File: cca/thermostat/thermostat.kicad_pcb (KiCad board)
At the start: 2 copper layers, 15 parts, among them K1 TX2-LT-5V-TH, K2 TX2-LT-5V-TH, K3 TX2-LT-5V-TH, Q1 2N3904, Q2 2N3904, Q3 2N3904, Q4 2N3904, Q5 2N3904, Q6 2N3904

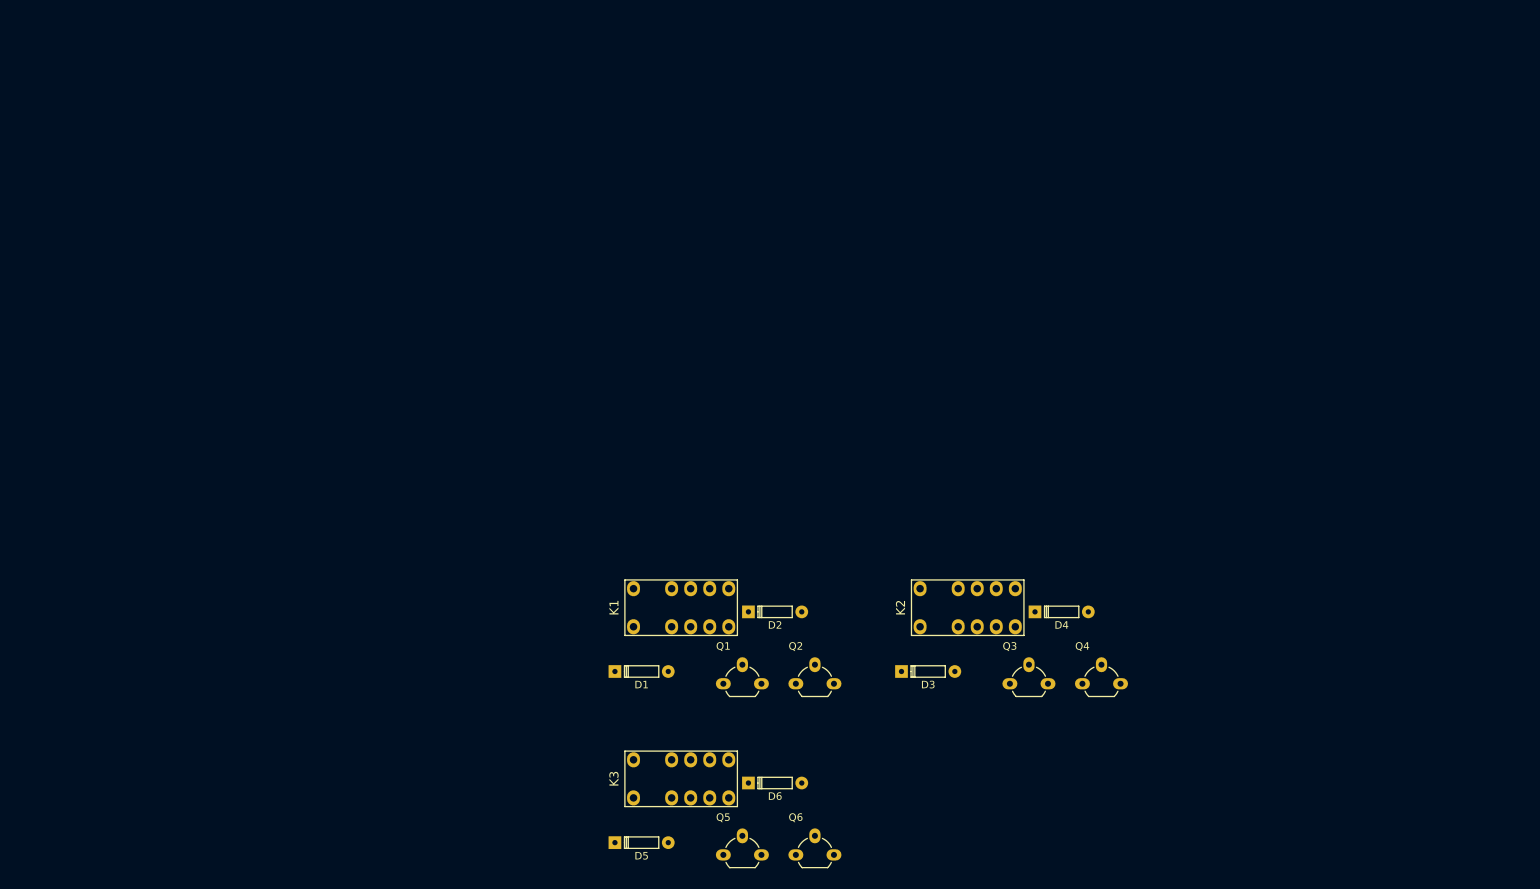
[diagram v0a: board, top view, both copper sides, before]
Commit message: Prelim schem. TODO: battery backup, layout
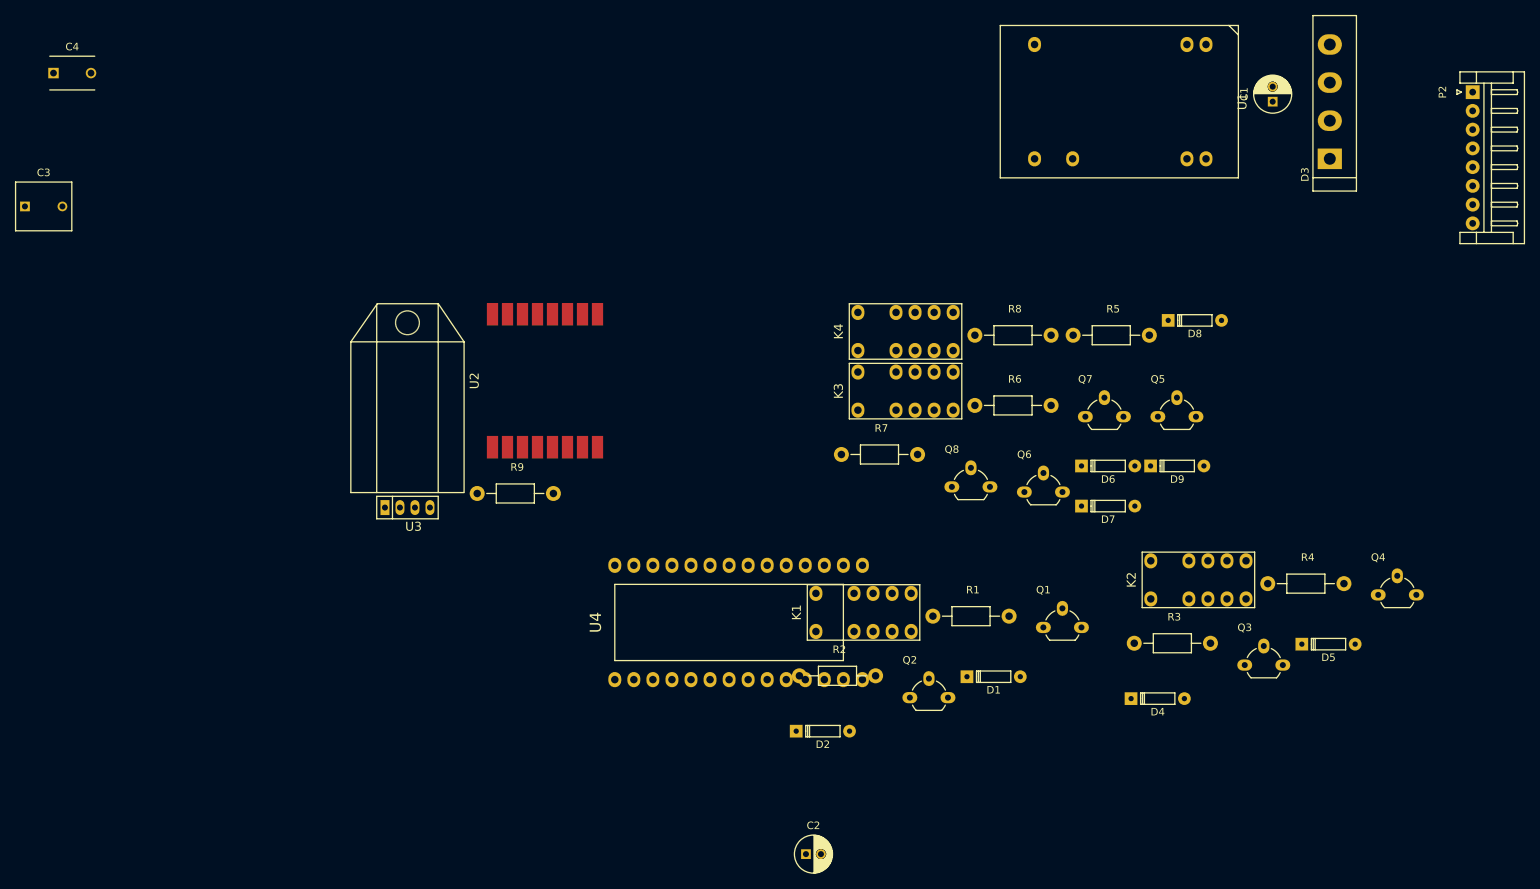
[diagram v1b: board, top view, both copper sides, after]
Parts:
- added C1: 47uF/63V, Capacitors_ThroughHole:C_Radial_D5_L11_P2, F.Cu at (233.7, 27.9)
- added C2: 10uF/16V, Capacitors_ThroughHole:C_Radial_D5_L11_P2, F.Cu at (171.4, 128.3)
- added C3: 1uF, Capacitors_ThroughHole:C_Rect_L7.5_W6.5_P5, F.Cu at (67.3, 41.9)
- added C4: 0.1uF, Capacitors_ThroughHole:C_Disc_D6_P5, F.Cu at (71.1, 24.1)
- added D7: 1N4148, t_footprints:DO-35, F.Cu at (208.2, 81.9)
- added D8: 1N4148, t_footprints:DO-35, F.Cu at (219.7, 57.1)
- added D9: 1N4148, t_footprints:DO-35, F.Cu at (217.4, 76.5)
- added K4: TX2-LT-5V-TH, t_footprints:RELAY_2_FORM_C, F.Cu at (178.4, 61.1)
- added P2: tstat_cable_con, JST_EH_RIGHT_8pin, F.Cu at (260.4, 26.7)
- added Q7: 2N3904, TO_SOT_Packages_THT:TO-92_Molded_Wide_Oval, F.Cu at (208.7, 69.9)
- added Q8: 2N3904, TO_SOT_Packages_THT:TO-92_Molded_Wide_Oval, F.Cu at (190.9, 79.3)
- added R1: 4.75k, Resistors_ThroughHole:Resistor_Horizontal_RM10mm, F.Cu at (188.4, 96.5)
- added R2: 4.75k, Resistors_ThroughHole:Resistor_Horizontal_RM10mm, F.Cu at (170.6, 104.5)
- added R3: 4.75K, Resistors_ThroughHole:Resistor_Horizontal_RM10mm, F.Cu at (215.2, 100.2)
- added R4: 4.75K, Resistors_ThroughHole:Resistor_Horizontal_RM10mm, F.Cu at (233.0, 92.2)
- added R5: 4.75K, Resistors_ThroughHole:Resistor_Horizontal_RM10mm, F.Cu at (207.1, 59.1)
- added R6: 4.75K, Resistors_ThroughHole:Resistor_Horizontal_RM10mm, F.Cu at (194.0, 68.4)
- added R7: 4.75K, Resistors_ThroughHole:Resistor_Horizontal_RM10mm, F.Cu at (176.2, 75.0)
- added R8: 4.75K, Resistors_ThroughHole:Resistor_Horizontal_RM10mm, F.Cu at (194.0, 59.1)
- added R9: 4.75K, Resistors_ThroughHole:Resistor_Horizontal_RM10mm, F.Cu at (127.6, 80.2)
- added U1: DJ06S4805A, DJ06S4805A, F.Cu at (224.8, 20.3)
- added U2: RFM69W, RFM69W, F.Cu at (129.7, 74.0)
- added U3: DHT22, DHT22, F.Cu at (115.3, 82.1)
- added U4: TEENSY-LC, Teensy-3.2, F.Cu at (148.5, 105.0)
- D3: value 1N4148 -> GBU806; footprint t_footprints:DO-35 -> GBU
- moved D5 95.3 mm to (237.6, 100.3)
- moved D3 89.1 mm to (241.3, 35.6), turned to 90 degrees
- moved Q5 82.3 mm to (218.4, 69.9)
- moved D6 61.3 mm to (208.2, 76.5)
- moved K3 59.7 mm to (178.4, 69.1)
- moved Q6 57.2 mm to (200.6, 80.0)
- moved D1 46.9 mm to (192.9, 104.6)
- moved Q1 43.3 mm to (203.1, 98.0)
- moved Q4 41.2 mm to (247.8, 93.7)
- moved Q3 31.4 mm to (230.0, 103.1)
- moved K2 31.0 mm to (217.4, 94.2)
- moved K1 24.3 mm to (172.8, 98.6)
- moved D4 17.3 mm to (214.8, 107.5)
- moved D2 17.1 mm to (170.1, 111.9)
- moved Q2 15.3 mm to (185.3, 107.4)
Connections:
- net /relay_heat.sch/R-COM renamed Net-(K3-Pad4)
- net /relay_heat.sch/R-NO renamed Net-(K3-Pad5)
- D3 pad 1: +5V -> Net-(C1-Pad1)
- D3 pad 2: Net-(D3-Pad2) -> /power/24VAC_2
- K1 pad 4: /relay_fan.sch/R-COM -> /power/24VAC_1
- K1 pad 5: /relay_fan.sch/R-NO -> /relay_fan/G
- K2 pad 12: Net-(D4-Pad2) -> Net-(D5-Pad2)
- K2 pad 4: /relay_cool.sch/R-COM -> /power/24VAC_1
- K2 pad 5: /relay_cool.sch/R-NO -> /relay_emheat/E
- K2 pad 7: Net-(D3-Pad2) -> Net-(D4-Pad2)
- K3 pad 1: +5V -> Net-(D6-Pad2)
- K3 pad 12: Net-(D6-Pad2) -> +5V
- K3 pad 6: +5V -> Net-(D8-Pad2)
- K3 pad 7: Net-(D5-Pad2) -> +5V
- K3 pad 9: Net-(K3-Pad9) -> /power/24VAC_1
- Q3 pad 3: Net-(D3-Pad2) -> Net-(D4-Pad2)
- Q4 pad 3: Net-(D4-Pad2) -> Net-(D5-Pad2)
- Q5 pad 3: Net-(D5-Pad2) -> Net-(D6-Pad2)
- Q6 pad 3: Net-(D6-Pad2) -> Net-(D7-Pad2)

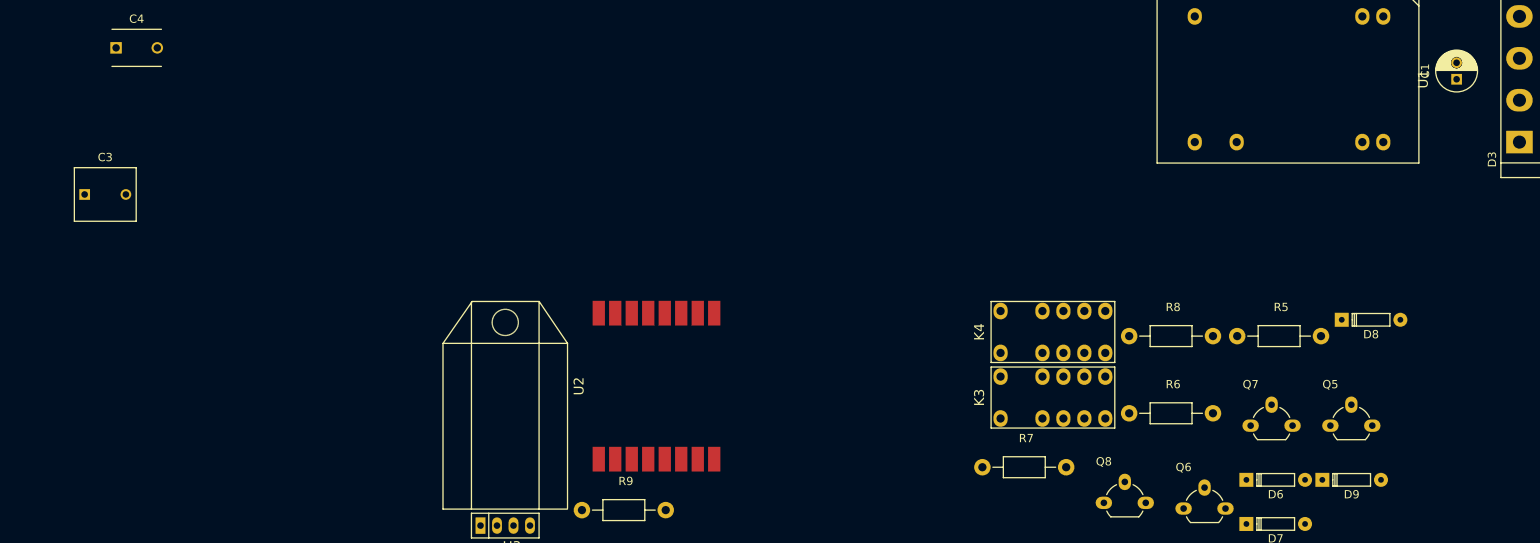
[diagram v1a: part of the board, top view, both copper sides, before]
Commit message: cap cleanup pass, fully qualify footprints
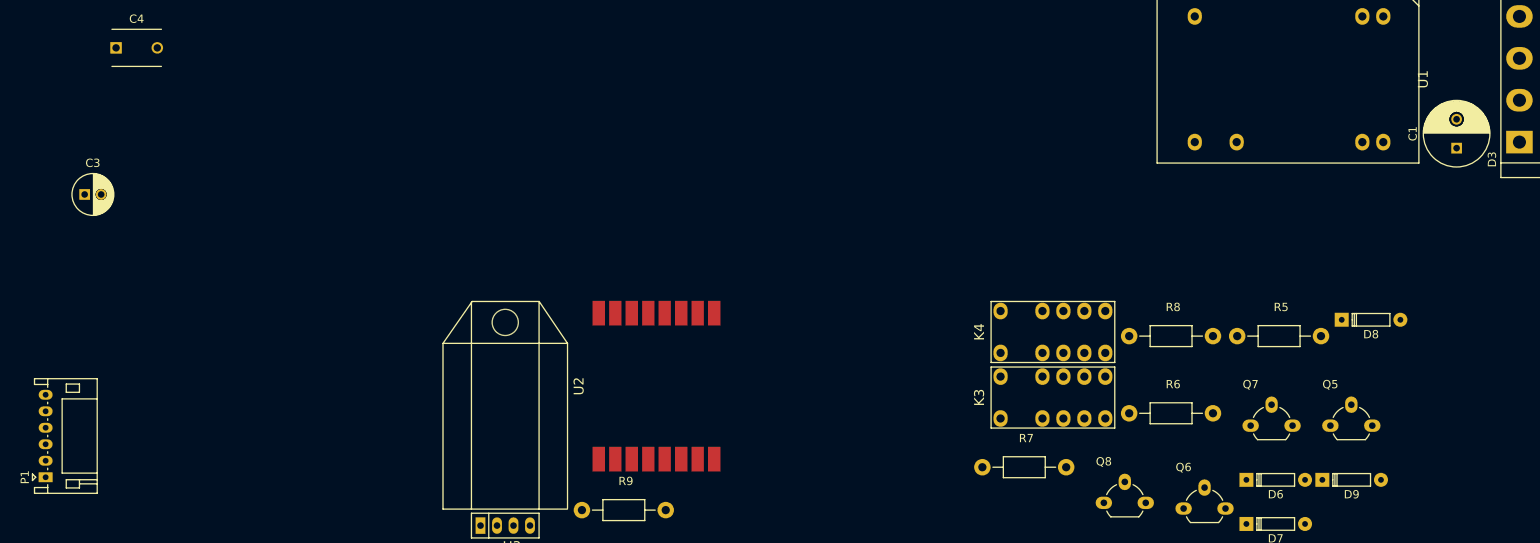
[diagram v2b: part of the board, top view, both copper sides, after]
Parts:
- added P1: tstat_ui_conn, t_footprints:JST_PH_RIGHT_6pin, F.Cu at (62.6, 76.2)
- C1: footprint Capacitors_ThroughHole:C_Radial_D5_L11_P2 -> t_footprints:C_Radial_D8_L15_P3.5
- C2: value 10uF/16V -> ESK106M016AC3AA; footprint Capacitors_ThroughHole:C_Radial_D5_L11_P2 -> t_footprints:C_Radial_D5_L12.5_P2
- C3: value 1uF -> 10uF/16V; footprint Capacitors_ThroughHole:C_Rect_L7.5_W6.5_P5 -> t_footprints:C_Radial_D5_L12.5_P2
- C4: value 0.1uF -> 0.1uF/50V
- D3: footprint GBU -> t_footprints:GBU
- P2: footprint JST_EH_RIGHT_8pin -> t_footprints:JST_EH_RIGHT_8pin
- moved C1 8.35 mm to (233.7, 36.3)
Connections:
- K1 pad 10: Net-(K1-Pad10) -> (no net)
- K1 pad 3: Net-(K1-Pad3) -> (no net)
- K1 pad 8: Net-(K1-Pad8) -> (no net)
- K1 pad 9: Net-(K1-Pad9) -> (no net)
- K2 pad 10: Net-(K2-Pad10) -> (no net)
- K2 pad 3: Net-(K2-Pad3) -> (no net)
- K2 pad 8: Net-(K2-Pad8) -> (no net)
- K2 pad 9: Net-(K2-Pad9) -> (no net)
- K3 pad 10: Net-(K3-Pad10) -> (no net)
- K3 pad 3: Net-(K3-Pad3) -> (no net)
- K3 pad 4: Net-(K3-Pad4) -> (no net)
- K3 pad 5: Net-(K3-Pad5) -> (no net)
- U1 pad 11: Net-(U1-Pad11) -> (no net)
- U2 pad 10: /control_comm/ant -> (no net)
- U2 pad 3: Net-(U2-Pad3) -> (no net)
- U2 pad 4: Net-(U2-Pad4) -> (no net)
- U2 pad 5: Net-(U2-Pad5) -> (no net)
- U2 pad 6: Net-(U2-Pad6) -> (no net)
- U2 pad 7: Net-(U2-Pad7) -> (no net)
- U3 pad 3: Net-(U3-Pad3) -> (no net)
- U4 pad 14: Net-(U4-Pad14) -> (no net)
- U4 pad 15: Net-(U4-Pad15) -> (no net)
- U4 pad 2: Net-(U4-Pad2) -> (no net)
- U4 pad 5: Net-(U4-Pad5) -> (no net)
- U4 pad 6: Net-(U4-Pad6) -> (no net)
- U4 pad 7: Net-(U4-Pad7) -> (no net)
- U4 pad 8: Net-(U4-Pad8) -> (no net)
- U4 pad 9: Net-(U4-Pad9) -> (no net)

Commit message: cleanup pass after clean checkout
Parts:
- C2: value ESK106M016AC3AA -> 10uF/16V
- moved C1 0.73 mm to (233.7, 35.6)
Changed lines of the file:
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@@
     (links 105)
     (no_connects 105)
-    (area 0 0 0 0)
+    (area 59.105 15.884999 269.553 133.145)
     (thickness 1.6)
     (drawings 0)
@@
   )
   (module t_footprints:C_Radial_D8_L15_P3.5 (layer F.Cu)
-    (at 233.68 36.29 90)
+    (at 233.68 35.56 90)
     (descr "Radial Electrolytic Capacitor Diameter 8mm x Length 15mm, Pitch 3.5mm")
     (tags "Electrolytic Capacitor")
@@
       (effects (font (size 1 1) (thickness 0.15)))
     )
-    (fp_text value ESK106M016AC3AA (at 1 3.8) (layer F.Fab)
-      (effects (font (size 1 1) (thickness 0.15)))
-    )
+    (fp_text value 10uF/16V (at 1 3.8) (layer F.Fab)
+      (effects (font (size 1 1) (thickness 0.15)))
+    )

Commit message: thermostat... wip many updates
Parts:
- added AE1: ANTENNA_915, t_footprints:ant_915_dipole_conn, F.Cu at (0.00, 0.00)
- P1: moved to B.Cu
- U1: footprint DJ06S4805A -> t_footprints:DJ06S4805A
- U2: footprint RFM69W -> t_footprints:RFM69W
- U3: footprint DHT22 -> t_footprints:DHT22
- U4: footprint Teensy-3.2 -> t_footprints:Teensy-3.2; moved to B.Cu
- moved U4 93.6 mm to (118.1, 16.5)
- moved P1 91.7 mm to (119.7, 4.45), turned to 0 degrees
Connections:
- P1 pad 3: /control_comm/ui_rx -> /control_comm/ui_tx
- P1 pad 5: /control_comm/ui_tx -> /control_comm/ui_rx
- U2 pad 10: (no net) -> /control_comm/ant
